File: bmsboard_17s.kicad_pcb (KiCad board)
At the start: 2 copper layers, 160 parts, among them Q1 Q_NMOS_GDS, Q10 Q_NMOS_GDS, Q11 Q_NMOS_GDS, Q12 Q_NMOS_GDS, Q13 Q_NMOS_GDS, Q14 Q_NMOS_GDS, Q15 Q_NMOS_GDS, Q16 Q_NMOS_GDS, Q17 Q_NMOS_GDS, Q18 Q_NMOS_GDS, Q19 Q_NMOS_GDS, Q2 Q_NMOS_GDS, Q20 Q_NMOS_GDS, Q21 Q_NMOS_GDS, Q22 Q_NMOS_GDS, Q23 Q_NMOS_GDS, Q24 Q_NMOS_GDS, Q25 Q_NMOS_GDS, Q26 Q_NMOS_GDS, Q3 Q_PMOS_GDS, Q4 Q_NPN_BCE, U1 PB7170P48, U10 TJA1042T-3, U2 CH32V103C8T6, U3 XTSD01G, U5 BMP280, U7 Si7020-A20, U8 QMA6100P, U9 ADS1243, Y1 16MHz, Y2 32.768kHz

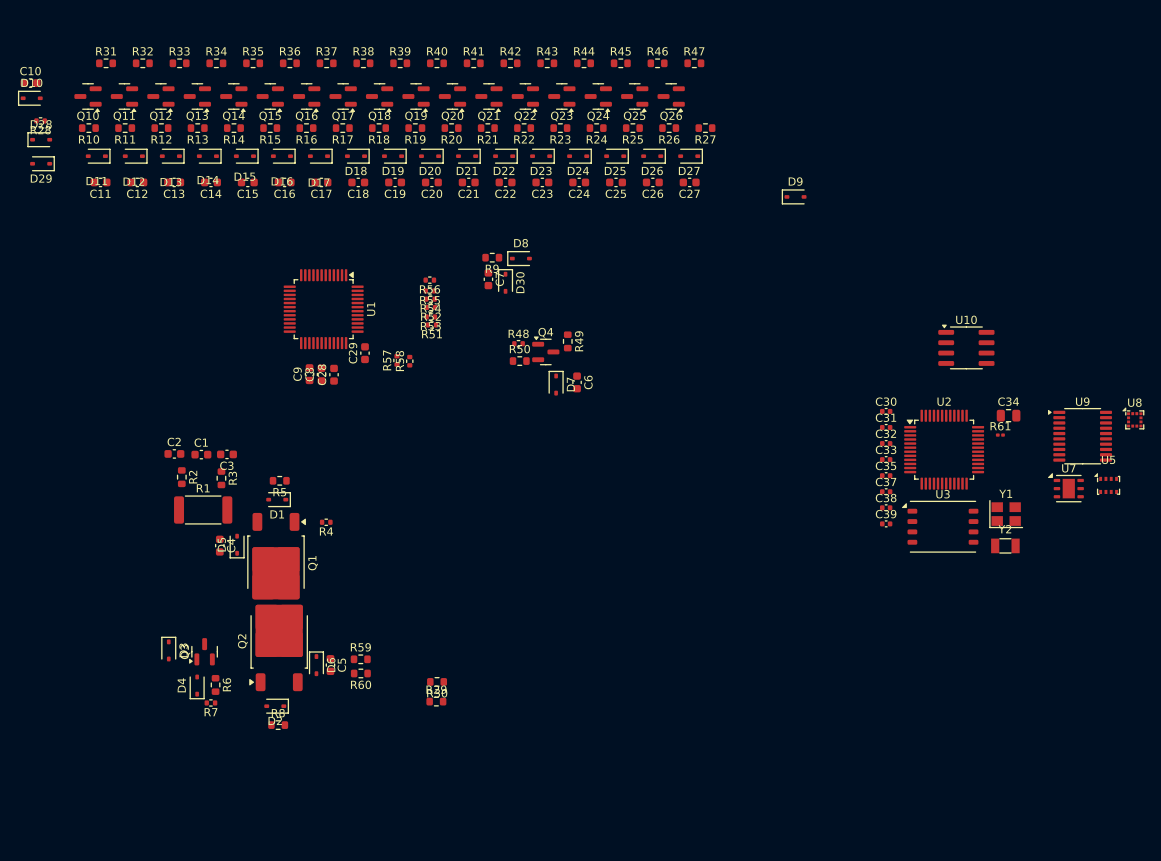
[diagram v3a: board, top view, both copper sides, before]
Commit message: AFE改为PB7170(LQFP-64)，修改原理图，调整元器件布局
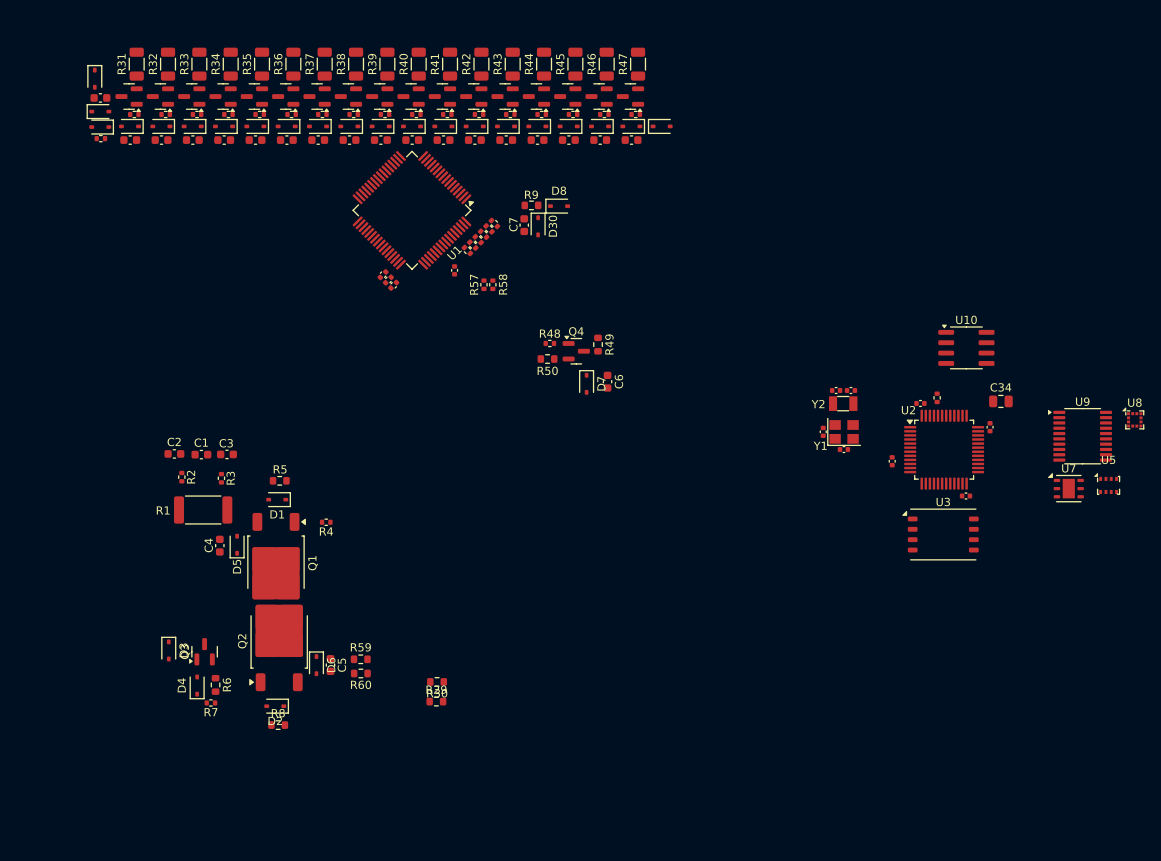
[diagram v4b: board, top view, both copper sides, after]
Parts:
- removed R27: 100, Resistor_SMD:R_0603_1608Metric
- C28, C29, C8, C9: footprint Capacitor_SMD:C_0603_1608Metric -> Capacitor_SMD:C_0402_1005Metric
- R10, R11, R12, R13, R14, R15, R16, R17, R18, R19, R2, R20, R21, R22, R23, R24, R25, R26, R3: footprint Resistor_SMD:R_0603_1608Metric -> Resistor_SMD:R_0402_1005Metric
- R31, R32, R33, R34, R35, R36, R37, R38, R39, R40, R41, R42, R43, R44, R45, R46, R47: footprint Resistor_SMD:R_0603_1608Metric -> Resistor_SMD:R_1206_3216Metric
- R61: footprint Resistor_SMD:R_0201_0603Metric -> Resistor_SMD:R_0402_1005Metric
- U1: value PB7170P48 -> PB7170; footprint Package_QFP:LQFP-48_7x7mm_P0.5mm -> Package_QFP:LQFP-64_10x10mm_P0.5mm
- moved Y2 26.5 mm to (117.1, 75.7), turned to 180 degrees
- moved Y1 22.3 mm to (117.2, 79.1)
- moved D9 18.6 mm to (94.9, 41.7)
- moved C39 17.4 mm to (135.1, 78.5), turned to -90 degrees
- moved U1 16.3 mm to (64.2, 52.0), turned to -135 degrees
- moved C9 15.2 mm to (60.7, 59.8), turned to 45 degrees
- moved C29 15.0 mm to (69.5, 59.3)
- moved C8 14.2 mm to (61.4, 60.5), turned to 45 degrees
- moved R57 14.1 mm to (73.1, 61.1)
- moved R58 13.8 mm to (74.2, 61.1)
- moved C38 13.5 mm to (126.6, 75.6)
- moved C28 13.2 mm to (62.0, 61.1), turned to 45 degrees
- moved R56 10.5 mm to (74.4, 53.6), turned to 135 degrees
- moved R55 10.5 mm to (73.7, 54.2), turned to 135 degrees
- moved C33 10.5 mm to (116.3, 74.0), turned to 180 degrees
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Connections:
- C11 pad 1: /AFE Module/C1 -> /AFE Module/BAT1
- C11 pad 2: /AFE Module/C0 -> /AFE Module/BAT0
- C12 pad 1: /AFE Module/C2 -> /AFE Module/BAT2
- C12 pad 2: /AFE Module/C1 -> /AFE Module/BAT1
- C13 pad 1: /AFE Module/C3 -> /AFE Module/BAT3
- C13 pad 2: /AFE Module/C2 -> /AFE Module/BAT2
- C14 pad 1: /AFE Module/C4 -> /AFE Module/BAT4
- C14 pad 2: /AFE Module/C3 -> /AFE Module/BAT3
- C15 pad 1: /AFE Module/C5 -> /AFE Module/BAT5
- C15 pad 2: /AFE Module/C4 -> /AFE Module/BAT4
- C16 pad 1: /AFE Module/C6 -> /AFE Module/BAT6
- C16 pad 2: /AFE Module/C5 -> /AFE Module/BAT5
- C17 pad 1: /AFE Module/C7 -> /AFE Module/BAT7
- C17 pad 2: /AFE Module/C6 -> /AFE Module/BAT6
- C18 pad 1: /AFE Module/C8 -> /AFE Module/BAT8
- C18 pad 2: /AFE Module/C7 -> /AFE Module/BAT7
- C19 pad 1: /AFE Module/C9 -> /AFE Module/BAT9
- C19 pad 2: /AFE Module/C8 -> /AFE Module/BAT8
- C20 pad 1: /AFE Module/C10 -> /AFE Module/BAT10
- C20 pad 2: /AFE Module/C9 -> /AFE Module/BAT9
- C21 pad 1: /AFE Module/C11 -> /AFE Module/BAT11
- C21 pad 2: /AFE Module/C10 -> /AFE Module/BAT10
- C22 pad 1: /AFE Module/C12 -> /AFE Module/BAT12
- C22 pad 2: /AFE Module/C11 -> /AFE Module/BAT11
- C23 pad 1: /AFE Module/C13 -> /AFE Module/BAT13
- C23 pad 2: /AFE Module/C12 -> /AFE Module/BAT12
- C24 pad 1: /AFE Module/C14 -> /AFE Module/BAT14
- C24 pad 2: /AFE Module/C13 -> /AFE Module/BAT13
- C25 pad 1: /AFE Module/C15 -> /AFE Module/BAT15
- C25 pad 2: /AFE Module/C14 -> /AFE Module/BAT14
- C26 pad 1: /AFE Module/C16 -> /AFE Module/BAT16
- C26 pad 2: /AFE Module/C15 -> /AFE Module/BAT15
- C27 pad 1: /AFE Module/C17 -> /AFE Module/BAT17
- C27 pad 2: /AFE Module/C16 -> /AFE Module/BAT16
- D10 pad 1: /AFE Module/C1 -> /AFE Module/BAT1
- D11 pad 1: /AFE Module/C1 -> /AFE Module/BAT1
- D11 pad 2: /AFE Module/C0 -> /AFE Module/BAT0
- D12 pad 1: /AFE Module/C2 -> /AFE Module/BAT2
- D12 pad 2: /AFE Module/C1 -> /AFE Module/BAT1
- D13 pad 1: /AFE Module/C3 -> /AFE Module/BAT3
- D13 pad 2: /AFE Module/C2 -> /AFE Module/BAT2
- D14 pad 1: /AFE Module/C4 -> /AFE Module/BAT4
- D14 pad 2: /AFE Module/C3 -> /AFE Module/BAT3
- D15 pad 1: /AFE Module/C5 -> /AFE Module/BAT5
- D15 pad 2: /AFE Module/C4 -> /AFE Module/BAT4
- D16 pad 1: /AFE Module/C6 -> /AFE Module/BAT6
- D16 pad 2: /AFE Module/C5 -> /AFE Module/BAT5
- D17 pad 1: /AFE Module/C7 -> /AFE Module/BAT7
- D17 pad 2: /AFE Module/C6 -> /AFE Module/BAT6
- D18 pad 1: /AFE Module/C8 -> /AFE Module/BAT8
- D18 pad 2: /AFE Module/C7 -> /AFE Module/BAT7
- D19 pad 1: /AFE Module/C9 -> /AFE Module/BAT9
- D19 pad 2: /AFE Module/C8 -> /AFE Module/BAT8
- D20 pad 1: /AFE Module/C10 -> /AFE Module/BAT10
- D20 pad 2: /AFE Module/C9 -> /AFE Module/BAT9
- D21 pad 1: /AFE Module/C11 -> /AFE Module/BAT11
- D21 pad 2: /AFE Module/C10 -> /AFE Module/BAT10
- D22 pad 1: /AFE Module/C12 -> /AFE Module/BAT12
- D22 pad 2: /AFE Module/C11 -> /AFE Module/BAT11
- D23 pad 1: /AFE Module/C13 -> /AFE Module/BAT13
- D23 pad 2: /AFE Module/C12 -> /AFE Module/BAT12
- D24 pad 1: /AFE Module/C14 -> /AFE Module/BAT14
- D24 pad 2: /AFE Module/C13 -> /AFE Module/BAT13
- D25 pad 1: /AFE Module/C15 -> /AFE Module/BAT15
- D25 pad 2: /AFE Module/C14 -> /AFE Module/BAT14
- D26 pad 1: /AFE Module/C16 -> /AFE Module/BAT16
- D26 pad 2: /AFE Module/C15 -> /AFE Module/BAT15
- D27 pad 1: /AFE Module/C17 -> /AFE Module/BAT17
- D27 pad 2: /AFE Module/C16 -> /AFE Module/BAT16
- D28 pad 2: /AFE Module/C0 -> /AFE Module/BAT0
- D29 pad 1: /AFE Module/C0 -> /AFE Module/BAT0
- Q10 pad 1: /AFE Module/C0 -> Net-(Q10-G)
- Q11 pad 1: /AFE Module/C1 -> Net-(Q11-G)
- Q12 pad 1: /AFE Module/C2 -> Net-(Q12-G)
- Q13 pad 1: /AFE Module/C3 -> Net-(Q13-G)
- Q14 pad 1: /AFE Module/C4 -> Net-(Q14-G)
- Q15 pad 1: /AFE Module/C5 -> Net-(Q15-G)
- Q16 pad 1: /AFE Module/C6 -> Net-(Q16-G)
- Q17 pad 1: /AFE Module/C7 -> Net-(Q17-G)
- Q18 pad 1: /AFE Module/C8 -> Net-(Q18-G)
- Q19 pad 1: /AFE Module/C9 -> Net-(Q19-G)
- Q20 pad 1: /AFE Module/C10 -> Net-(Q20-G)
- Q21 pad 1: /AFE Module/C11 -> Net-(Q21-G)
- Q22 pad 1: /AFE Module/C12 -> Net-(Q22-G)
- Q23 pad 1: /AFE Module/C13 -> Net-(Q23-G)
- Q24 pad 1: /AFE Module/C14 -> Net-(Q24-G)
- Q25 pad 1: /AFE Module/C15 -> Net-(Q25-G)
- Q26 pad 1: /AFE Module/C16 -> Net-(Q26-G)
- R10 pad 1: /AFE Module/C0 -> Net-(Q10-G)
- R10 pad 2: /AFE Module/BAT0 -> /AFE Module/S1
- R11 pad 1: /AFE Module/C1 -> Net-(Q11-G)
- R11 pad 2: /AFE Module/BAT1 -> /AFE Module/S2
- R12 pad 1: /AFE Module/C2 -> Net-(Q12-G)
- R12 pad 2: /AFE Module/BAT2 -> /AFE Module/S3
- R13 pad 1: /AFE Module/C3 -> Net-(Q13-G)
- R13 pad 2: /AFE Module/BAT3 -> /AFE Module/S4
- R14 pad 1: /AFE Module/C4 -> Net-(Q14-G)
- R14 pad 2: /AFE Module/BAT4 -> /AFE Module/S5
- R15 pad 1: /AFE Module/C5 -> Net-(Q15-G)
- R15 pad 2: /AFE Module/BAT5 -> /AFE Module/S6
- R16 pad 1: /AFE Module/C6 -> Net-(Q16-G)
- R16 pad 2: /AFE Module/BAT6 -> /AFE Module/S7
- R17 pad 1: /AFE Module/C7 -> Net-(Q17-G)
- R17 pad 2: /AFE Module/BAT7 -> /AFE Module/S8
- R18 pad 1: /AFE Module/C8 -> Net-(Q18-G)
- R18 pad 2: /AFE Module/BAT8 -> /AFE Module/S9
- R19 pad 1: /AFE Module/C9 -> Net-(Q19-G)
- R19 pad 2: /AFE Module/BAT9 -> /AFE Module/S10
- R20 pad 1: /AFE Module/C10 -> Net-(Q20-G)
- R20 pad 2: /AFE Module/BAT10 -> /AFE Module/S11
- R21 pad 1: /AFE Module/C11 -> Net-(Q21-G)
- R21 pad 2: /AFE Module/BAT11 -> /AFE Module/S12
- R22 pad 1: /AFE Module/C12 -> Net-(Q22-G)
- R22 pad 2: /AFE Module/BAT12 -> /AFE Module/S13
- R23 pad 1: /AFE Module/C13 -> Net-(Q23-G)
- R23 pad 2: /AFE Module/BAT13 -> /AFE Module/S14
- R24 pad 1: /AFE Module/C14 -> Net-(Q24-G)
- R24 pad 2: /AFE Module/BAT14 -> /AFE Module/S15
- R25 pad 1: /AFE Module/C15 -> Net-(Q25-G)
- R25 pad 2: /AFE Module/BAT15 -> /AFE Module/S16
- R26 pad 1: /AFE Module/C16 -> Net-(Q26-G)
- R26 pad 2: /AFE Module/BAT16 -> /AFE Module/S17
- R28 pad 1: /AFE Module/C0 -> /AFE Module/BAT0
- U1 pad 10: /AFE Module/C9 -> /AFE Module/BAT13
- U1 pad 11: /AFE Module/C8 -> /AFE Module/S13
- U1 pad 12: /AFE Module/C7 -> /AFE Module/BAT12
- U1 pad 13: /AFE Module/C6 -> /AFE Module/S12
- U1 pad 14: /AFE Module/C5 -> /AFE Module/BAT11
- U1 pad 15: /AFE Module/C4 -> /AFE Module/S11
- U1 pad 16: /AFE Module/C3 -> /AFE Module/BAT10
- U1 pad 17: /AFE Module/C2 -> /AFE Module/S10
- U1 pad 18: /AFE Module/C1 -> /AFE Module/BAT9
- U1 pad 19: /AFE Module/C0 -> /AFE Module/S9
- U1 pad 2: /AFE Module/C17 -> /AFE Module/BAT17
- U1 pad 20: GND -> /AFE Module/BAT8
- U1 pad 21: /AFE Module/SRP -> /AFE Module/S8
- U1 pad 22: /AFE Module/SRN -> /AFE Module/BAT7
- U1 pad 23: /AFE Module/DSG -> /AFE Module/S7
- U1 pad 24: unconnected-(U1-PREMOS-Pad24) -> /AFE Module/BAT6
- U1 pad 25: /AFE Module/CHG -> /AFE Module/S6
- U1 pad 26: /AFE Module/LODD -> /AFE Module/BAT5
- U1 pad 27: /AFE Module/CHGD -> /AFE Module/S5
- U1 pad 28: GNDA -> /AFE Module/BAT4
- U1 pad 29: Net-(U1-VREF) -> /AFE Module/S4
- U1 pad 3: /AFE Module/C16 -> /AFE Module/S17
- U1 pad 30: Net-(U1-AVDD) -> /AFE Module/BAT3
- U1 pad 31: Net-(U1-VAA) -> /AFE Module/S3
- U1 pad 32: unconnected-(U1-AUXIN5-Pad32) -> /AFE Module/BAT2
- U1 pad 33: unconnected-(U1-AUXIN4-Pad33) -> /AFE Module/S2
- U1 pad 34: unconnected-(U1-AUXIN3-Pad34) -> /AFE Module/BAT1
- U1 pad 35: unconnected-(U1-AUXIN2-Pad35) -> /AFE Module/S1
- U1 pad 36: unconnected-(U1-AUXIN1-Pad36) -> /AFE Module/BAT0
- U1 pad 37: /AFE Module/DRIVE -> GND
- U1 pad 38: unconnected-(U1-ACT-Pad38) -> /AFE Module/SRP
- U1 pad 39: Net-(U1-DVDD) -> /AFE Module/SRN
- U1 pad 4: /AFE Module/C15 -> /AFE Module/BAT16
- U1 pad 40: Net-(U1-ALERT) -> /AFE Module/DSG
- U1 pad 42: Net-(U1-GPIO1) -> /AFE Module/CHG
- U1 pad 43: Net-(U1-GPIO2) -> /AFE Module/LODD
- U1 pad 44: Net-(U1-SDO) -> /AFE Module/CHGD
- U1 pad 45: Net-(U1-SDI) -> GNDA
- U1 pad 46: Net-(U1-CSN) -> Net-(U1-VREF)
- U1 pad 47: Net-(U1-SCLK) -> Net-(U1-AVDD)
- U1 pad 48: GND -> Net-(U1-VAA)
- U1 pad 5: /AFE Module/C14 -> /AFE Module/S16
- U1 pad 6: /AFE Module/C13 -> /AFE Module/BAT15
- U1 pad 7: /AFE Module/C12 -> /AFE Module/S15
- U1 pad 8: /AFE Module/C11 -> /AFE Module/BAT14
- U1 pad 9: /AFE Module/C10 -> /AFE Module/S14
- Y1 pad 3: Net-(U2-PD1) -> GND
- Y1 pad 4: GND -> Net-(U2-PD1)

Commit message: 充放电MOS管改为6个并联
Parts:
- added Q29: Q_NMOS_GDS, Package_TO_SOT_SMD:TO-252-2, F.Cu at (61.2, 107.4)
- added Q30: Q_NMOS_GDS, Package_TO_SOT_SMD:TO-252-2, F.Cu at (61.1, 96.5)
- added Q31: Q_NMOS_GDS, Package_TO_SOT_SMD:TO-252-2, F.Cu at (78.8, 107.4)
- added Q32: Q_NMOS_GDS, Package_TO_SOT_SMD:TO-252-2, F.Cu at (69.9, 96.5)
- added Q33: Q_NMOS_GDS, Package_TO_SOT_SMD:TO-252-2, F.Cu at (70.0, 107.4)
- added Q34: Q_NMOS_GDS, Package_TO_SOT_SMD:TO-252-2, F.Cu at (78.7, 96.5)
- added Q35: Q_NMOS_GDS, Package_TO_SOT_SMD:TO-252-2, F.Cu at (87.6, 107.4)
- added Q36: Q_NMOS_GDS, Package_TO_SOT_SMD:TO-252-2, F.Cu at (87.5, 96.5)
- added Q37: Q_NMOS_GDS, Package_TO_SOT_SMD:TO-252-2, F.Cu at (96.4, 107.4)
- added Q38: Q_NMOS_GDS, Package_TO_SOT_SMD:TO-252-2, F.Cu at (96.3, 96.5)
- added R27: 1k, Resistor_SMD:R_0603_1608Metric, F.Cu at (48.2, 112.3)
- added R88: 1k, Resistor_SMD:R_0603_1608Metric, F.Cu at (57.0, 112.3)
- added R89: 1k, Resistor_SMD:R_0603_1608Metric, F.Cu at (74.6, 112.3)
- added R90: 1k, Resistor_SMD:R_0603_1608Metric, F.Cu at (65.8, 112.3)
- added R91: 1k, Resistor_SMD:R_0603_1608Metric, F.Cu at (83.4, 112.3)
- added R92: 1k, Resistor_SMD:R_0603_1608Metric, F.Cu at (92.2, 112.3)
- added R93: 1k, Resistor_SMD:R_0603_1608Metric, F.Cu at (56.5, 91.6)
- added R94: 1k, Resistor_SMD:R_0603_1608Metric, F.Cu at (65.3, 91.6)
- added R95: 1k, Resistor_SMD:R_0603_1608Metric, F.Cu at (74.1, 91.6)
- added R96: 1k, Resistor_SMD:R_0603_1608Metric, F.Cu at (82.9, 91.6)
- added R97: 1k, Resistor_SMD:R_0603_1608Metric, F.Cu at (91.7, 91.6)
- added R98: 1k, Resistor_SMD:R_0603_1608Metric, F.Cu at (100.5, 91.6)
- R4: value 1k -> 100; footprint Resistor_SMD:R_0402_1005Metric -> Resistor_SMD:R_0603_1608Metric
- moved R30 27.8 mm to (43.3, 123.8)
- moved R29 26.9 mm to (46.4, 129.2)
- moved R60 18.3 mm to (42.0, 99.9), turned to 0 degrees
- moved R59 16.9 mm to (42.0, 101.6), turned to 180 degrees
- moved D6 10.7 mm to (42.0, 106.2)
- moved C5 10.7 mm to (43.7, 106.2)
- moved R4 8.76 mm to (53.8, 81.5), turned to -90 degrees
- moved D2 6.64 mm to (51.2, 118.3)
- moved R8 5.95 mm to (51.1, 120.0)
- moved Q2 5.20 mm to (52.5, 107.4)
- moved Q1 4.92 mm to (52.3, 96.5)
- moved D1 2.68 mm to (50.3, 86.9)
- moved R5 2.34 mm to (50.4, 85.2)
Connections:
- net Net-(D1-A) renamed /AFE Module/SW_INNER
- net Net-(D5-K) renamed /AFE Module/SW_MID
- D1 pad 1: Net-(D1-K) -> /AFE Module/MOSG_DSG
- D2 pad 2: Net-(D2-A2) -> /AFE Module/MOSG_CHG
- Q1 pad 1: Net-(D1-K) -> Net-(Q1-G)
- Q2 pad 1: Net-(D2-A2) -> Net-(Q2-G)
- R4 pad 2: Net-(D1-K) -> /AFE Module/MOSG_DSG
- R5 pad 1: Net-(D1-K) -> /AFE Module/MOSG_DSG
- R6 pad 2: Net-(D2-A2) -> /AFE Module/MOSG_CHG
- R7 pad 1: Net-(D2-A2) -> /AFE Module/MOSG_CHG
- R8 pad 1: Net-(D2-A2) -> /AFE Module/MOSG_CHG
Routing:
- added copper zone on B.Cu, net /AFE Module/PACK-
- added copper zone on F.Cu, net /AFE Module/PACK-
- added copper zone on B.Cu, net /AFE Module/SW_INNER
- added copper zone on F.Cu, net /AFE Module/SW_INNER
- added copper zone on B.Cu, net /AFE Module/SW_MID
- added copper zone on F.Cu, net /AFE Module/SW_MID

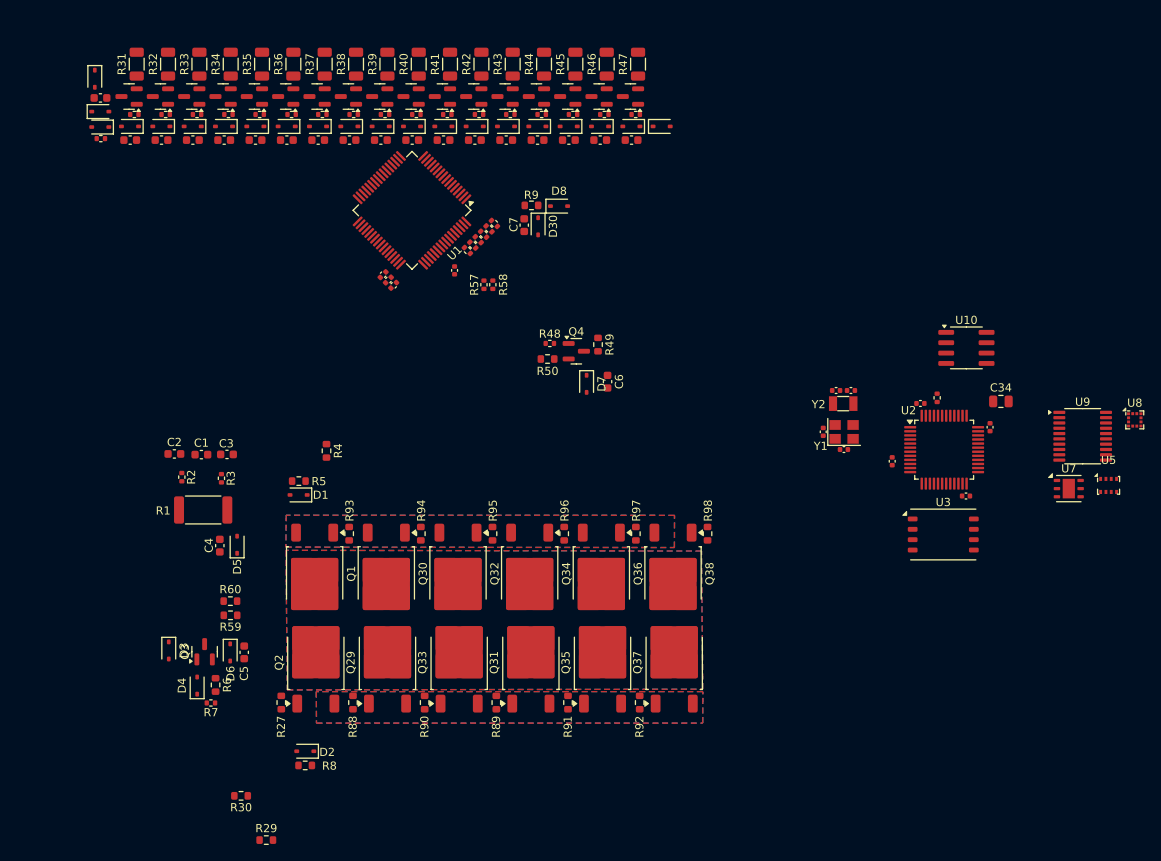
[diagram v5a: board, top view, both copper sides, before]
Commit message: 添加部分布线（电压、电流采样和MOS管控制），划定外框
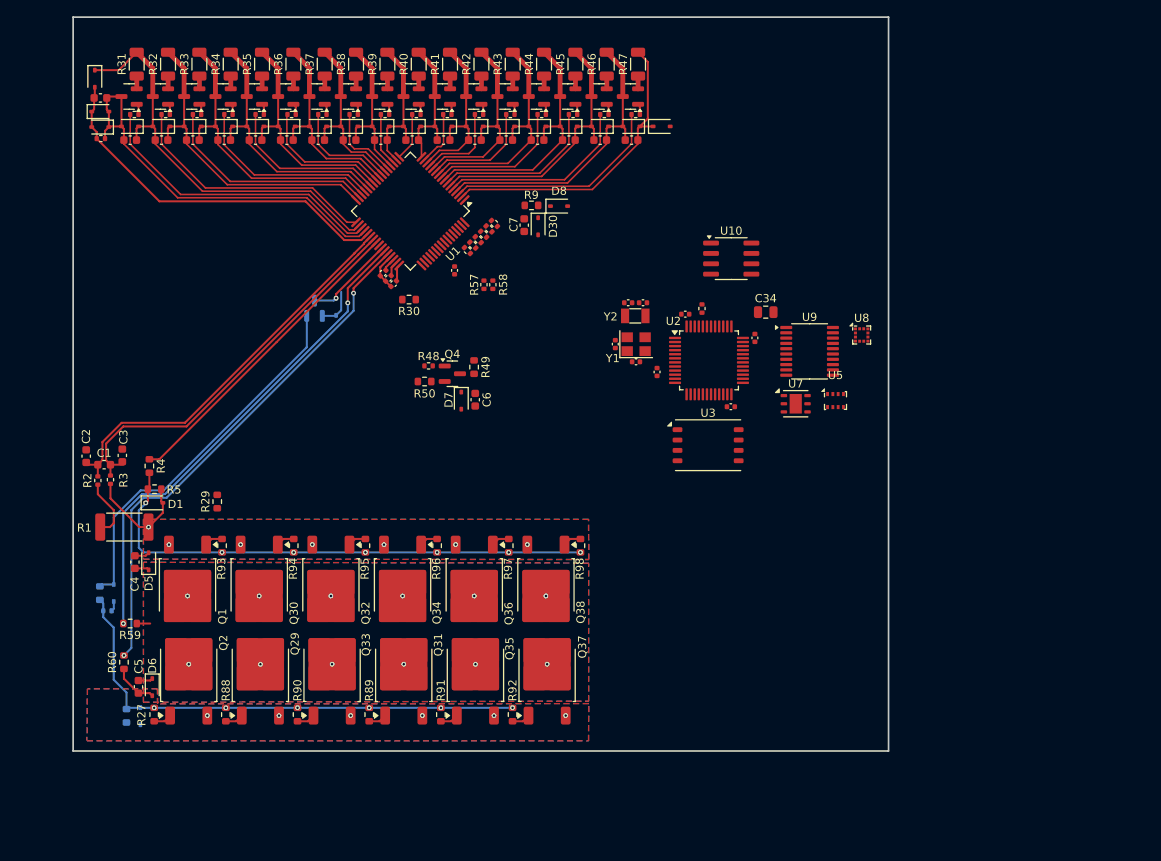
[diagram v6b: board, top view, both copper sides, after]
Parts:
- D2, D3, D4, Q3, R6, R7, R8: moved to B.Cu
- moved R30 64.3 mm to (63.9, 62.9)
- moved D3 46.9 mm to (54.9, 63.8)
- moved Q3 44.2 mm to (52.3, 64.0)
- moved R29 41.9 mm to (40.4, 87.7), turned to 90 degrees
- moved U5 35.1 mm to (116.2, 75.3)
- moved U9 35.1 mm to (113.0, 69.2)
- moved U8 35.1 mm to (119.4, 67.2)
- moved U7 35.1 mm to (111.3, 75.7)
- moved U10 30.8 mm to (103.4, 57.9)
- moved C34 30.8 mm to (107.6, 64.4)
- moved C35 30.8 mm to (94.3, 71.8)
- moved C37 30.8 mm to (103.3, 76.0)
- moved R61 30.8 mm to (99.8, 64.0)
- moved U3 30.8 mm to (100.6, 80.8)
- moved C38 30.8 mm to (97.8, 64.7)
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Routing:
- net /AFE Module/CHGD: track 0.00 -> 64.3 mm, vias 0 -> 2
- net /AFE Module/MOSG_DSG: track 0.00 -> 64.1 mm, vias 0 -> 7
- net /AFE Module/MOSG_CHG: track 0.00 -> 62.2 mm, vias 0 -> 6
- net /AFE Module/LODD: track 0.00 -> 60.6 mm, vias 0 -> 2
- net /AFE Module/BAT1: track 0.00 -> 51.3 mm
- net GND: track 0.00 -> 50.3 mm
- net /AFE Module/SRP: track 0.00 -> 49.3 mm
- net /AFE Module/BAT0: track 0.00 -> 49.2 mm
- net /AFE Module/SRN: track 0.00 -> 48.9 mm
- net Net-(D4-A): track 0.00 -> 46.2 mm
- net /AFE Module/BAT2: track 0.00 -> 39.3 mm
- net /AFE Module/DSG: track 0.00 -> 38.8 mm
- net /AFE Module/BAT17: track 0.00 -> 38.2 mm
- net /AFE Module/S1: track 0.00 -> 36.8 mm
- net /AFE Module/BAT16: track 0.00 -> 36.6 mm
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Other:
- board outline added: 100 x 90 mm
